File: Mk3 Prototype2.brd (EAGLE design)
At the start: 119.6 x 67.6 mm, 193 parts, among them IC1 BD49XXX, IC2 NCP1529MU, IC3 STM32F401V, IC4 CC3100, IC5 S25FL216K0PMFI011, IC6 CC3100MOD, IC7 BQ2970, J1 ZX62-AB-5PA(11), J2 ER-TFT024-3, J3 SWD_SHROUD, Q1 DMMT5401, Q2 NTR4101, Q3 NTR4101, Q5 NTR4101, Q6 NTR4101, SW1 JOYSTICK_MINI_MULTICOMP, U3 MCP73831, U4 USD-SOCKETNEW, X1 ESP-07, X2 16MHz-3.2-2.5, X3 ABS07-32.768KHZ-T, X4 DNP - ABS07-32.768KHZ-T, X5 Q24FA20H00396, X6 MC-921

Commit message: some more routing
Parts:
- removed Q5: NTR4101, TiLDA Mk3 Parts:SOT23-R
- added C48: 0603/100n/??/X5R, TiLDA Mk3 Parts:C0603K-SMALL
- added JP4: TC2030-SWDNL, tag-connect:TC2030-MCP-NL
- added Q8: (no value), TiLDA Mk3 Parts:SOT23-3
- added R50: 2k2, TiLDA Mk3 Parts:C0603K-SMALL
- added R51: 330, TiLDA Mk3 Parts:C0603K-SMALL
- C45: value 0402/100n/10V/X5R -> 0402/100n/6.3V/X5R; device TiLDA Mk3 Parts:C0402-SMALLER -> TiLDA Mk3 Parts:C0603K-SMALL
- Q3: value NTR4101 -> (none); device TiLDA Mk3 Parts:SOT23-R -> TiLDA Mk3 Parts:SOT23-3
- R17, R20: device TiLDA Mk3 Parts:R0402-SMALLER -> TiLDA Mk3 Parts:C0603K-SMALL
- TP1, TP10, TP2, TP3, TP4, TP5, TP6, TP7, TP8, TP9: value TP3MM -> TP3.5MMEDGE; device TiLDA Mk3 Parts:3MMEDGE -> TiLDA Mk3 Parts:3.5MMEDGE
- moved Q4 81.7 mm to (54.8, 52.0), flipped to the bottom, turned to 270 degrees
- moved Q7 81.4 mm to (51.2, 52.0), flipped to the bottom, turned to 90 degrees
- moved IC7 81.2 mm to (53.2, 55.2), flipped to the bottom
- moved R2 60.6 mm to (4.40, 8.40)
- moved LED5 54.9 mm to (24.7, 5.00), turned to 90 degrees
- moved Q3 39.5 mm to (11.2, 51.6), turned to 0 degrees
- moved R17 35.0 mm to (92.9, 16.9), turned to 90 degrees
- moved IC1 34.8 mm to (31.8, 77.0), turned to 180 degrees
- moved C7 32.6 mm to (36.1, 76.5)
- moved C2 31.9 mm to (39.2, 75.6)
- moved R7 31.6 mm to (36.4, 74.3)
- moved R44 21.4 mm to (74.4, 59.2)
- moved R49 18.2 mm to (72.8, 59.2)
- moved J3 15.8 mm to (22.8, 55.1)
- moved R48 15.1 mm to (71.2, 59.2)
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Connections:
- removed net N$61: Q5.3, R1.2
- removed net TIM4_CH2: IC3.60
- removed net TIM4_CH3: IC3.61
- removed net TIM9_CH1: Q3.1
- removed net VSS: IC7.4
- new net BOOT1: IC3.37, R11.2
- new net N$45: Q4.3, Q7.3
- new net N$50: IC7.2, Q4.1
- new net N$55: IC7.3, Q7.1
- new net N$57: C48.1, IC7.4, JP3.1, Q7.2
- new net N$62: JP3.2, R51.2
- new net N$63: IC7.6, R50.1
- new net N$64: Q8.3, R44.1, R47.1, R48.1, R49.1
- new net TIM4_CH4: IC3.62, Q8.1
- net +3V3: now also J2.1, JP4.1, R1.2; no longer Q3.2, Q5.2
- net ESP_CH_PD: now also IC3.39; no longer IC3.37, R11.2
- net GND: now also JP4.5, Q3.2, Q4.2, Q8.2, R50.2; no longer JP3.1, LED1.K, R44.1, R47.1, R48.1, R49.1
- net N$14: now also LED1.K; no longer J2.1
- net NRST: now also JP4.3
- net SDIO_SW: now also IC3.67; no longer IC3.62
- net SWCLK: now also JP4.4
- net SWDAT: now also JP4.2
- net TIM1_CH1N: now also Q3.1; no longer Q5.1
- net VBAT: now also C48.2, IC7.5, R51.1; no longer JP3.2
- net V_UNREG: now also IC2.6
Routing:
- net +3V3: track 21.6 -> 208.3 mm, vias 0 -> 7
- net TIM4_CH4: track 0.00 -> 115.4 mm, vias 0 -> 8
- net CHARGING: track 0.00 -> 113.0 mm, vias 0 -> 3
- net VBUS: track 11.0 -> 97.5 mm
- net GND: track 61.1 -> 140.8 mm, vias 12 -> 28
- net ESP_CH_PD: track 39.3 -> 106.3 mm
- net VBAT: track 20.2 -> 79.8 mm, vias 0 -> 2
- net V_UNREG: track 17.1 -> 64.1 mm, vias 0 -> 2
- net TIM10_CH1: track 0.00 -> 44.0 mm, vias 0 -> 2
- net TIM11_CH1: track 0.00 -> 38.4 mm, vias 0 -> 2
- net SWCLK: track 8.73 -> 40.9 mm
- net SWDAT: track 12.6 -> 42.2 mm, vias 2 -> 4
- net SPI3_SCK: track 15.6 -> 43.7 mm, vias 0 -> 2
- net LCD_RD: track 10.3 -> 37.4 mm, vias 0 -> 2
- net COMMAND: track 9.61 -> 36.4 mm, vias 0 -> 2
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- added copper zone on layer 1, net N$53
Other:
- board size 119.6 x 67.6 mm -> 119.6 x 68 mm

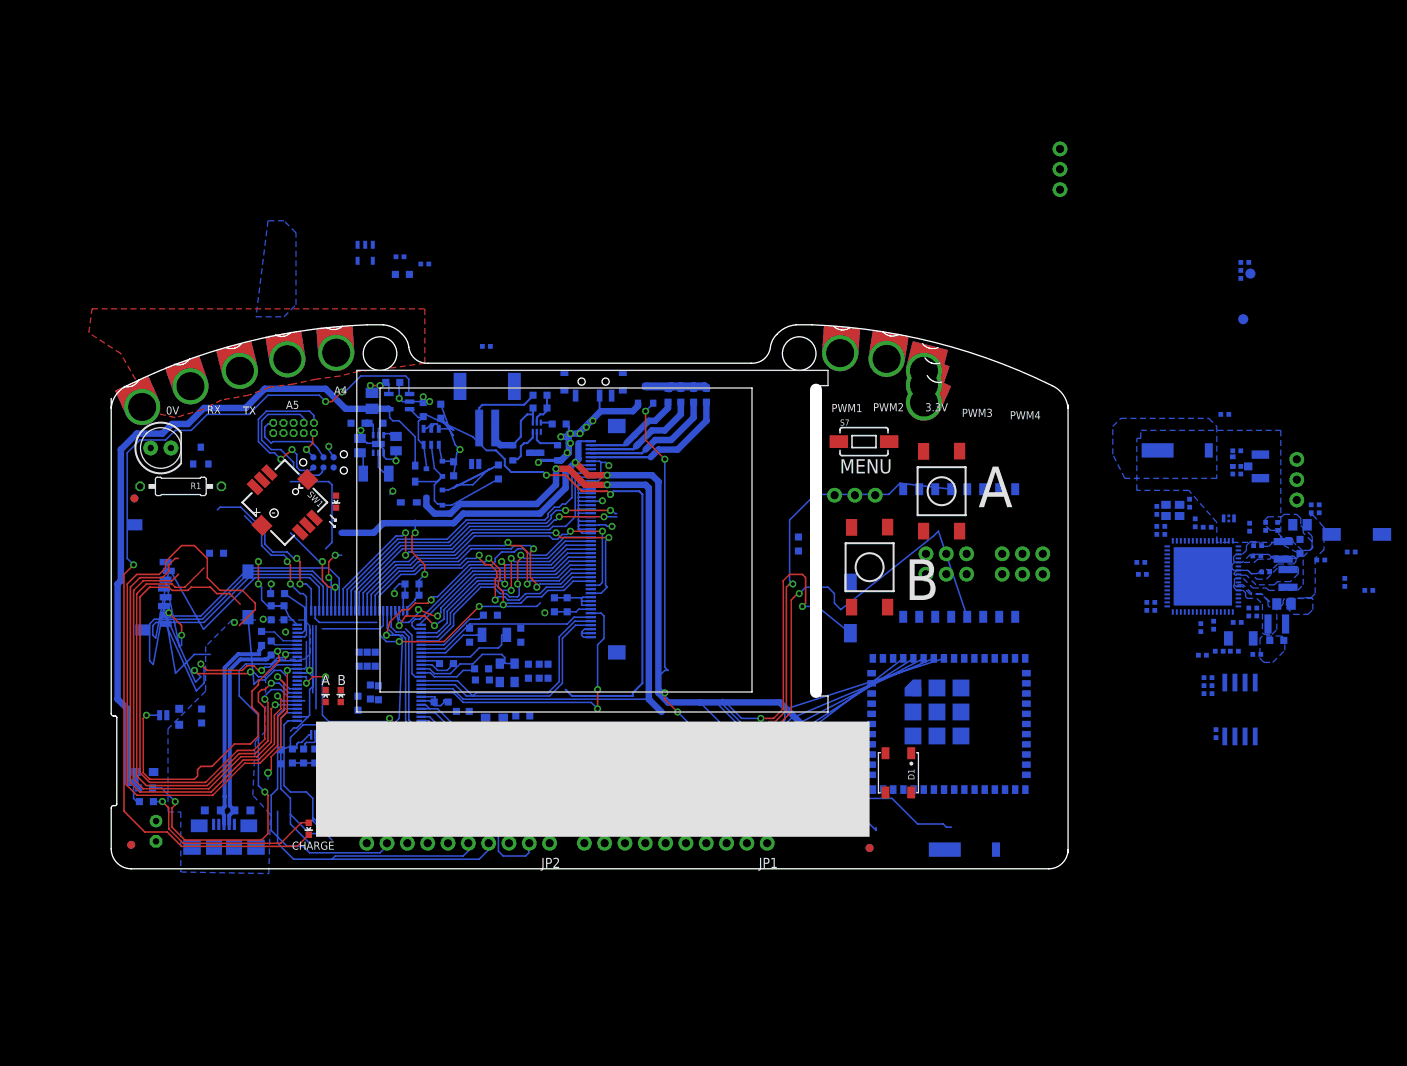
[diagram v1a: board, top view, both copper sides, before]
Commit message: aligning some parts better
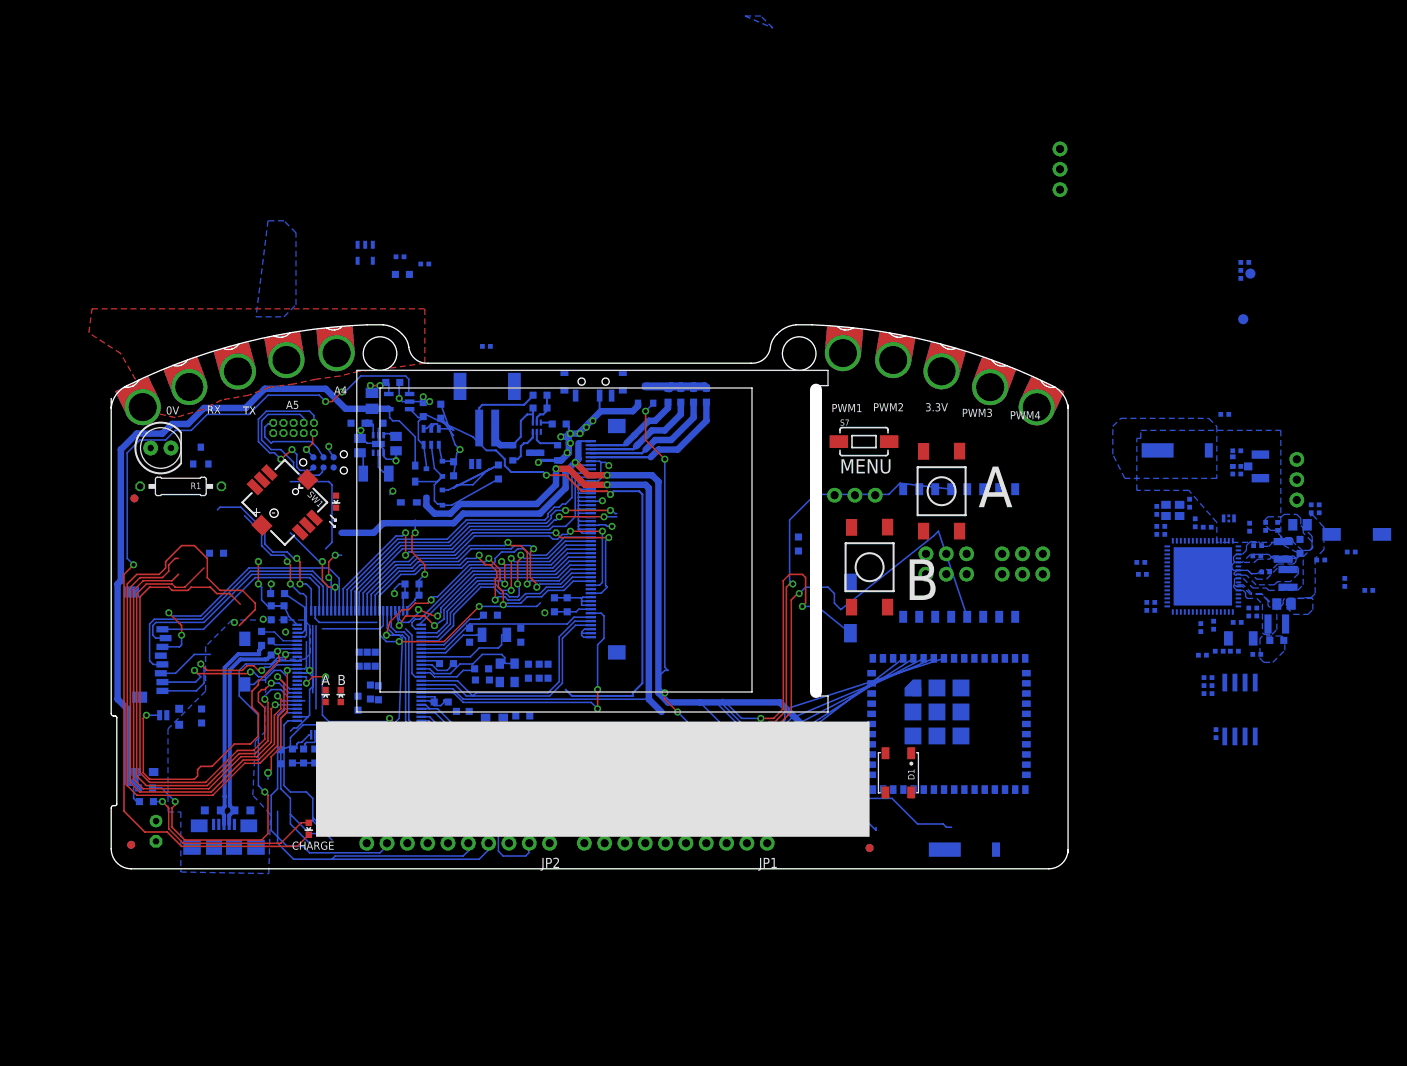
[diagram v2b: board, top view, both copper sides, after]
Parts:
- moved TP10 14.2 mm to (117.1, 60.6), turned to 334.6 degrees
- moved U4 8.41 mm to (17.1, 21.0)
- moved TP9 8.36 mm to (111.0, 63.2), turned to 339.6 degrees
- moved TP6 2.28 mm to (104.7, 65.3), turned to 344.6 degrees
- moved TP4 0.86 mm to (98.3, 66.8), turned to 350.2 degrees
- moved TP3 0.40 mm to (91.8, 67.7), turned to 355 degrees
- moved TP2 0.34 mm to (15.0, 65.3), turned to 15.4 degrees
- moved TP1 0.26 mm to (8.62, 63.3), turned to 20.4 degrees
- moved TP7 0.18 mm to (21.4, 66.8), turned to 9.8 degrees
- moved TP5 0.05 mm to (2.55, 60.6), turned to 25.4 degrees
- turned TP8 to 5 degrees
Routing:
- net SDIO_CLK: track 42.6 -> 35.2 mm
- net SDIO_D3: track 37.9 -> 30.6 mm
- net SDIO_SW: track 13.6 -> 6.36 mm
- net GND: track 140.8 -> 134.1 mm
- net SDIO_CMD: track 42.1 -> 35.7 mm
- net SDIO_D0: track 25.2 -> 20.2 mm
- net SDIO_D1: track 26.5 -> 21.5 mm
- net SDIO_D2: track 30.2 -> 25.7 mm
- added copper zone on layer 16, net GND1

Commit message: started to rework pin mapping a little so the lcd uses the FSMC pins
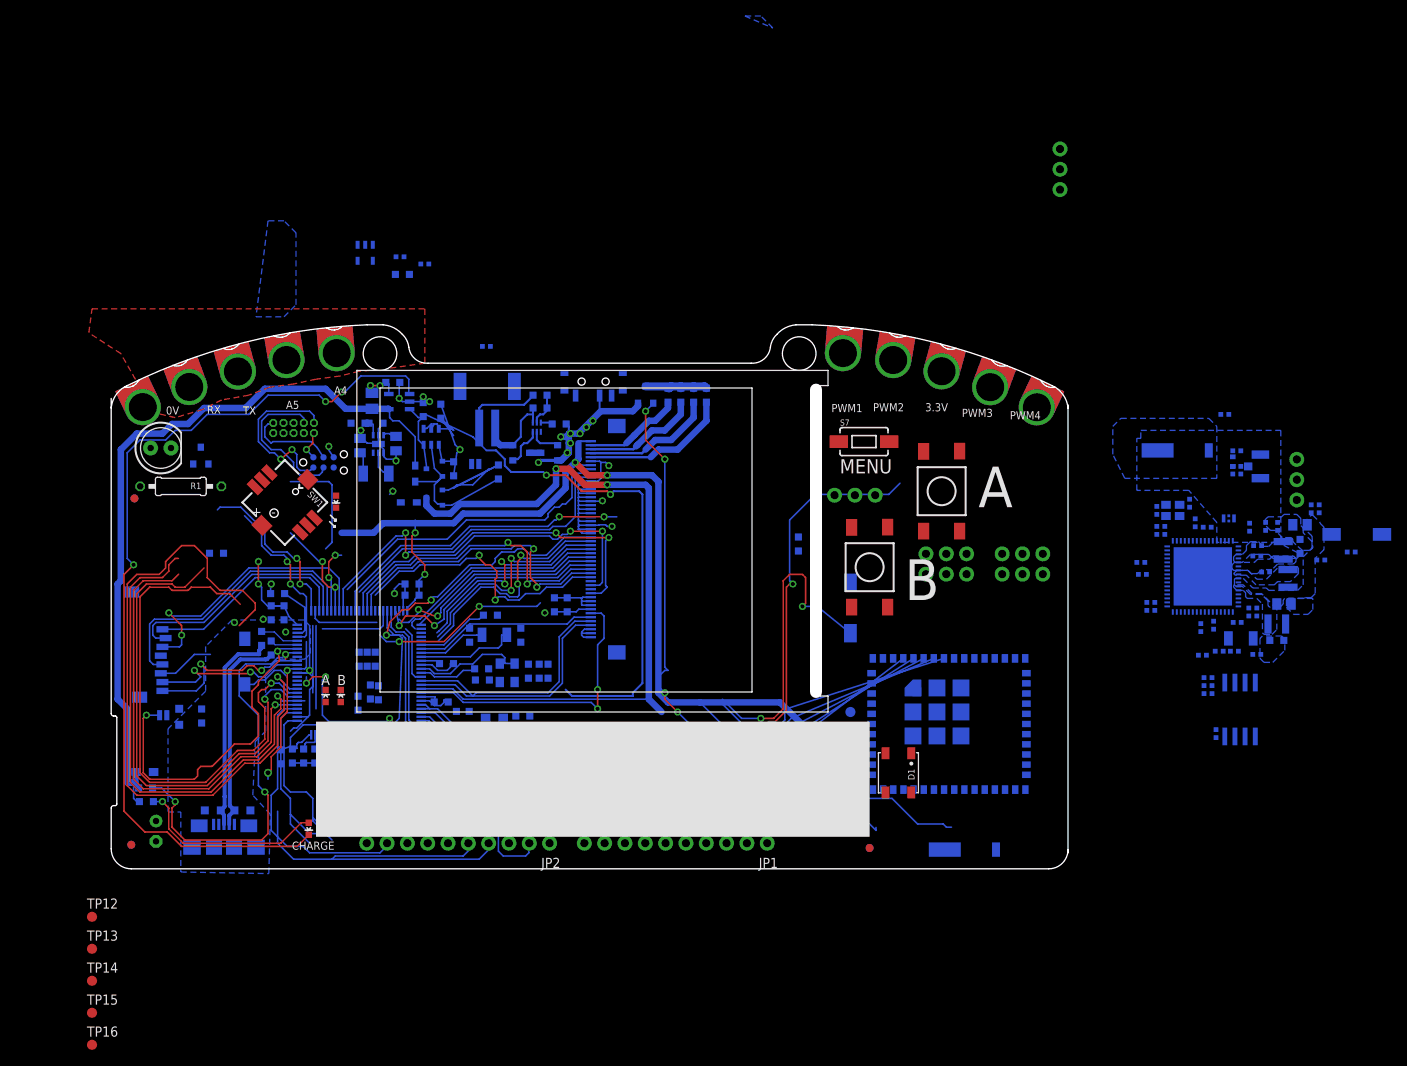
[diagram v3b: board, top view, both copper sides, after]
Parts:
- removed C41: 0402/4u7/6.3V/X5R, TiLDA Mk3 Parts:C0402-SMALLER
- removed R13: 0402/0.1R/5%, TiLDA Mk3 Parts:R0402-SMALLER
- removed R29, R30: 0402/100K/5%, TiLDA Mk3 Parts:R0402-SMALLER
- removed TP11: TPB1,27, TiLDA Mk3 Parts:B1,27
- removed X1: ESP-07, TiLDA Mk3 Parts:ESP-07
- added TP12, TP13, TP15, TP16, TP17: TPB1,27, TiLDA Mk3 Parts:B1,27
- moved TP14 169.7 mm to (-2.40, -14.0), flipped to the top, turned to 0 degrees
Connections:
- removed net COMMAND: IC3.93, J2.36
- removed net ESP_CH_PD: IC3.39, IC6.35, S8.1, X1.3
- removed net VCC: C41.2, R13.2, TP14.TP, X1.8
- new net CC_RST: IC6.35, S8.1
- new net LCD_WRX: IC3.86, J2.36
- new net N$61: IC6.48, TP14.TP
- new net N$65: IC6.49, TP15.TP
- new net N$66: IC6.50, TP16.TP
- new net N$67: IC6.52, TP17.TP
- net +3V3: no longer R13.1, R29.1, TP11.TP
- net BTN_MENU: no longer IC3.82
- net CC_HIB: no longer X1.12
- net CC_IRQ: no longer X1.4
- net GND: no longer C41.1, R30.1, X1.9
- net LCD0: now also IC3.61; no longer IC3.97
- net LCD1: now also IC3.62; no longer IC3.98
- net LCD2: now also IC3.81; no longer IC3.1
- net LCD3: now also IC3.82; no longer IC3.2
- net LCD4: now also IC3.38; no longer IC3.3
- net LCD5: now also IC3.39; no longer IC3.4
- net LCD6: now also IC3.40; no longer IC3.5
- net LCD7: now also IC3.41; no longer IC3.38
- net LCD_!RST: no longer IC3.88
- net LCD_MODE: no longer IC3.85
- net LCD_RD: now also IC3.85; no longer IC3.92
- net MOM_DWN: no longer IC3.41
- net MOM_RIGHT: no longer IC3.81
- net N$39: now also IC6.51, TP12.TP; no longer R29.2, X1.11
- net N$44: now also IC6.44, TP13.TP; no longer R30.2, X1.10
- net TIM1_CH1: no longer IC3.40
- net TIM4_CH4: no longer IC3.62
- net USART2_RX: no longer X1.16
- net USART2_TX: no longer IC3.86, X1.15
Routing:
- net ESP_CH_PD: track 106.3 -> 0.00 mm, vias 2 -> 0
- net LCD5: track 30.7 -> 95.6 mm
- net CC_IRQ: track 89.9 -> 28.6 mm, vias 2 -> 0
- net MOM_DWN: track 55.1 -> 0.00 mm
- net LCD7: track 51.5 -> 105.6 mm
- net USART2_TX: track 40.3 -> 0.00 mm, vias 2 -> 0
- net CC_RST: track 0.00 -> 39.3 mm, vias 0 -> 2
- net COMMAND: track 36.4 -> 0.00 mm, vias 2 -> 0
- net BTN_MENU: track 12.8 -> 0.00 mm, vias 2 -> 0
- net LCD3: track 27.6 -> 39.7 mm, vias 0 -> 2
- net MOM_RIGHT: track 8.21 -> 0.00 mm, vias 2 -> 0
- net LCD2: track 25.2 -> 33.2 mm, vias 0 -> 2
- net CC_HIB: track 140.3 -> 133.9 mm
- net TIM1_CH1: track 64.4 -> 61.7 mm
- net LCD_MODE: track 44.2 -> 41.5 mm
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
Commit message: some poking
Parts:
- moved TP16 99.3 mm to (90.0, 14.4), flipped to the bottom
- moved TP15 98.5 mm to (91.2, 12.8), flipped to the bottom
- moved TP12 95.9 mm to (90.8, 16.4), flipped to the bottom
- moved TP14 95.7 mm to (90.0, 10.8), flipped to the bottom
- moved TP13 95.5 mm to (91.2, 9.20), flipped to the bottom
- moved TP17 2.68 mm to (90.0, 18.4)
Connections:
- net USART2_RX: no longer IC3.87
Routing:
- net USART2_RX: track 39.0 -> 0.00 mm, vias 2 -> 0
- net +3V3: track 208.3 -> 205.1 mm

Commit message: more part specing
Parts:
- removed ANT2: CHIPANT, TiLDA Mk3 Parts:2450AT42A100
- removed C28, C49: 0603/10u/6.3V/X5R, TiLDA Mk3 Parts:C0603K-SMALL
- removed C30, C31, C32, C36, C42, C44, C50, C56, C62, C64, C69: 0402/100n/10V/X5R, TiLDA Mk3 Parts:C0402-SMALLER
- removed C35, C43, C47: 0402/4u7/6.3V/X5R, TiLDA Mk3 Parts:C0402-SMALLER
- removed C40: 0805/22u/??V/X5R, passives-7351:C0805-N
- removed C46, C55: 0402/1u/10V/X5R, TiLDA Mk3 Parts:C0402-SMALLER
- removed C65, C68: 0402/6p2/100V/NP0, TiLDA Mk3 Parts:C0402-SMALLER
- removed C67: 0402/1p/50V/NP0, TiLDA Mk3 Parts:C0402-SMALLER
- removed C70: 0402/??/50V/NP0, TiLDA Mk3 Parts:C0402-SMALLER
- removed FL1: DEA202450BT-1294C1-H, TiLDA Mk3 Parts:DEA202450BT
- removed IC4: CC3100, TiLDA Mk3 Parts:VQFN-64
- removed IC5: S25FL216K0PMFI011, TiLDA Mk3 Parts:SO08-EIAJ
- removed L4, L6: 1008/2u2/1300mA, TiLDA Mk3 Parts:1008
- removed L5: 1008/1u/1500mA, TiLDA Mk3 Parts:1008
- removed L7: 0402/??, TiLDA Mk3 Parts:L0402
- removed R24: 0, TiLDA Mk3 Parts:R0402-SMALLER
- removed R26, R27, R28, R31, R34, R35, R36, R38, R39, R40, R42: 0402/100K/5%, TiLDA Mk3 Parts:R0402-SMALLER
- removed R32: 0402/12R/5%, TiLDA Mk3 Parts:R0402-SMALLER
- removed R37, R46: 0402/10K/5%, TiLDA Mk3 Parts:R0402-SMALLER
- removed R41: DNP (0ohm), TiLDA Mk3 Parts:R0402-SMALLER
- removed R7: 0402/47k/5%, TiLDA Mk3 Parts:C0603K-SMALL
- removed R8: 0402/90k/1%, TiLDA Mk3 Parts:C0603K-SMALL
- removed R9: 0402/22k/1%, TiLDA Mk3 Parts:C0603K-SMALL
- removed S6: SWITCH-MOMENTARY-2SMD-1101NE, SparkFun-Electromechanical:TACTILE-SWITCH-1101NE
- removed SV1: (no value), TiLDA Mk3 Parts:1X03
- removed X4: DNP - ABS07-32.768KHZ-T, TiLDA Mk3 Parts:RESONATOR_EPSON_FC_145
- removed X5: Q24FA20H00396, TiLDA Mk3 Parts:CRYSTAL-2.5X2.0
- removed X6: MC-921, con-coax:MC-921
- removed Z1, Z2, Z3: VARISTORCN0603, TiLDA Mk3 Parts:CT/CN0603
- C1: device TiLDA Mk3 Parts:C0805K -> TiLDA Mk3 Parts:C0603K-SMALL
- C10: value 0402/0R -> 0603/0R
- C11, C12, C16, C19, C22, C34, C39: value 0402/100n/10V/X5R -> 0603/100n/10V/X5R
- C13, C14, C18, C33: value 0402/1u/10V/X5R -> 0603/1u/10V/X5R
- C15: value 0402/10n/25V/X7R -> 0603/10n/25V/X7R
- C2: value 0402/4u7/6.3V/X5R -> 0603/1u/10V/X5R; device TiLDA Mk3 Parts:C0402-SMALLER -> TiLDA Mk3 Parts:C0603K-SMALL
- C20, C21, C23, C24: value 0402/10p/50V/NP0 -> 0603/10p/50V/NP0
- C25, C26: value DNP - 0402/10p/50V/NP0 -> 1210/100u/20%; device TiLDA Mk3 Parts:C0402-SMALLER -> TiLDA Mk3 Parts:C1210K
- C27: value 0805/22u/??V/X5R -> 0805/10u/10V/X5R
- C29, C9: value 0402/2.2u/6.3V/X5R -> 0603/2.2u/6.3V/X5R
- C38, C8: value 0402/4u7/6.3V/X5R -> 0603/4u7/10V/X5R
- C45: value 0402/100n/6.3V/X5R -> 0603/100n/10V/X5R
- C48: value 0603/100n/??/X5R -> 0603/100n/10V/X5R
- C7: value 0402/10n/25V/X7R -> 0603/100n/10V/X5R; device TiLDA Mk3 Parts:C0402-SMALLER -> TiLDA Mk3 Parts:C0603K-SMALL
- IC1: value BD49XXX -> TPD3E001DRL; device TiLDA Mk3 Parts:SSOP5 -> TiLDA Mk3 Parts:DRL-5
- IC2: value NCP1529MU -> TPS62082; device TiLDA Mk3 Parts:DFN6 -> TiLDA Mk3 Parts:WSON8
- R10: value 0402/1k/5% -> 0603/1k/5%
- R11, R20, R33: value 0402/100K/5% -> 0603/100K/5%
- R15: value 0402/47k/5% -> 0603/47k/5%
- R16: value 0402/10k/5% -> 0603/10k/5%
- R17: value 0402/10K/5% -> 0603/10k/5%
- R18, R19, R3, R4, R45: value 0402/220k/5% -> 0603/220k/5%
- R21, R22: value 0402/220K/5% -> 0603/220k/5%
- R23, R25: value 0402/22/1% -> 0603/22/1%
- R43: value 0402/220/5% -> 0603/220/5%
- R44, R47, R48, R49: value (none) -> 0603/4.7/5%
- R5: value 0402/2M2/5% -> 0603/2M2/5%
- R50: value 2k2 -> 0603/2k/5%
- R6: value 0402/2k/5% -> 0603/2k/5%
- moved C27 113.8 mm to (33.6, 46.8)
- moved C2 90.7 mm to (-2.00, -5.20), flipped to the top, turned to 0 degrees
- moved IC1 70.5 mm to (14.0, 8.80), turned to 0 degrees
- moved C7 69.5 mm to (16.0, 10.0), turned to 270 degrees
- moved C25 62.8 mm to (82.8, 9.60), turned to 90 degrees
- moved C26 56.4 mm to (86.8, 9.60), turned to 90 degrees
- moved R17 14.5 mm to (86.1, 4.10)
- moved C5 4.80 mm to (35.9, 52.9)
- moved C6 4.42 mm to (31.2, 52.8)
- moved TP17 2.80 mm to (90.0, 15.6)
- moved TP12 2.33 mm to (92.0, 14.4)
- moved TP16 1.20 mm to (90.0, 13.2)
- moved TP15 1.13 mm to (92.0, 12.0)
- moved TP13 0.89 mm to (92.0, 9.60)
- moved L1 0.60 mm to (33.7, 49.4), turned to 180 degrees
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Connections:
- removed net ANT: ANT2.P$1, C70.1, L7.2
- removed net CC_FLASH_!CS: IC4.14, IC5.1, R40.2
- removed net CC_FLASH_CLK: IC4.11, IC5.6, R39.1
- removed net CC_FLASH_MISO: IC4.13, IC5.2
- removed net CC_FLASH_MOSI: IC4.12, IC5.5, R31.1
- removed net MCO1: R24.1
- removed net N$10: IC4.3, R27.1
- removed net N$11: IC4.19, R34.1
- removed net N$12: C7.1, IC1.1
- removed net N$13: IC2.1, R8.2, R9.1
- removed net N$16: IC4.38, L6.2
- removed net N$17: C27.2, C40.2, C55.2, IC4.33, IC4.42
- removed net N$18: C36.2, C49.2, C50.2, C56.2, IC4.25, IC4.36, IC4.48, L6.1
- removed net N$19: IC4.43, L4.2
- removed net N$20: C62.2, IC4.24
- removed net N$22: C28.2, C30.2, C42.2, IC4.56, IC4.9, L4.1
- removed net N$23: IC4.40, L5.2
- removed net N$24: IC4.41, L5.1
- removed net N$25: C32.2, IC4.49
- removed net N$26: IC2.5, L1.1
- removed net N$3: FL1.IN, IC4.31
- removed net N$32: C25.2, IC4.51, R24.2, X4.P$2
- removed net N$40: IC4.55, R46.2, SV1.3
- removed net N$48: R41.1, X6.1
- removed net N$5: C26.2, IC4.52, R26.2, X4.P$1
- removed net N$56: C2.1, IC1.2, R7.2
- removed net N$8: C65.2, IC4.22, X5.3
- removed net N$9: C68.2, IC4.23, X5.1
- removed net USART2_RX: R46.1
- removed net USART2_TX: IC4.57, SV1.2
- removed net WIFI_!HIB: IC4.2
- removed net WIFI_!RESET: C64.2, IC4.32, R38.2, S6.1
- removed net WIFI_FORCE_AP: IC4.4, R28.1
- removed net WIFI_INTR: IC4.15, R42.1
- removed net WIFI_SOP0: IC4.35, R35.1
- removed net WIFI_SOP1: IC4.34, R36.1
- removed net WIFI_SOP2: IC4.21, R37.1
- net +3V3: now also C2.2, C25.1, C26.1, C27.1, IC2.5; no longer C31.2, C35.2, C43.2, C44.2, C46.2, C47.2, C69.2, IC4.10, IC4.37, IC4.39, IC4.44, IC4.54, IC5.3, IC5.7, IC5.8, R26.1, R38.1, R40.1, R8.1
- net GND: now also C2.1, C25.2, C26.2, C27.2, C7.1, IC2.3; no longer C2.2, C25.1, C26.1, C27.1, C28.1, C30.1, C31.1, C32.1, C35.1, C36.1, C40.1, C42.1, C43.1, C44.1, C46.1, C47.1, C49.1, C50.1, C55.1, C56.1, C62.1, C64.1, C65.1, C67.2, C68.1, C69.1, C7.2, C70.2, FL1.GND@2, FL1.GND@4, IC2.4, IC4.PAD, IC5.4, R27.2, R28.2, R31.2, R34.2, R35.2, R36.2, R37.2, R39.2, R42.2, R9.2, S6.2, SV1.1, X5.2, X5.4, X6.2@1, X6.2@2, Z1.2, Z2.2, Z3.2
- net N$2: now also IC2.7, L1.1; no longer C67.1, FL1.OUT, L7.1, R41.2
- net N$27: now also C7.2, IC1.5
- net USB_D_N: now also IC1.1; no longer Z2.1
- net USB_D_P: now also IC1.2; no longer Z3.1
- net USB_ID: now also IC1.4; no longer Z1.1
- net V_UNREG: now also IC2.1, IC2.8; no longer IC2.3, IC2.6, R7.1
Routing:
- net TIM1_CH3: track 90.8 -> 127.9 mm
- net TIM1_CH1: track 61.7 -> 90.4 mm
- net CC_IRQ: track 28.6 -> 57.2 mm
- net N$27: track 0.00 -> 26.0 mm, vias 0 -> 2
- net TIM1_CH2: track 59.7 -> 85.0 mm
- net +3V3: track 205.1 -> 227.1 mm
- net N$61: track 0.00 -> 10.4 mm
- net N$66: track 0.00 -> 10.2 mm
- net N$67: track 0.00 -> 9.77 mm
- net N$65: track 0.00 -> 8.39 mm
- net N$39: track 0.00 -> 7.74 mm
- net GND: track 134.1 -> 127.1 mm
- net USB_ID: track 0.00 -> 6.97 mm, vias 0 -> 2
- net N$44: track 0.00 -> 3.84 mm
- net N$26: track 3.43 -> 0.00 mm
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- removed copper zone on layer 16, net N$16
- removed copper zone on layer 16, net N$17
- removed copper zone on layer 16, net N$18
- removed copper zone on layer 16, net N$19
- removed copper zone on layer 16, net N$23
- removed copper zone on layer 16, net N$29
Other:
- outline, holes or cut-outs redrawn
